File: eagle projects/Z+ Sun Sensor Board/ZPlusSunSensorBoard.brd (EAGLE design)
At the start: 78 x 78 mm, 51 parts, among them Q2 BSS138, Q4 BSS138, Q6 BSS138, Q8 BSS138, U1 ADS7841E_2K5, U2 REF194GSZ-REEL7, U3 TLV9054IDR, U4 LM20BIM7X_NOPB

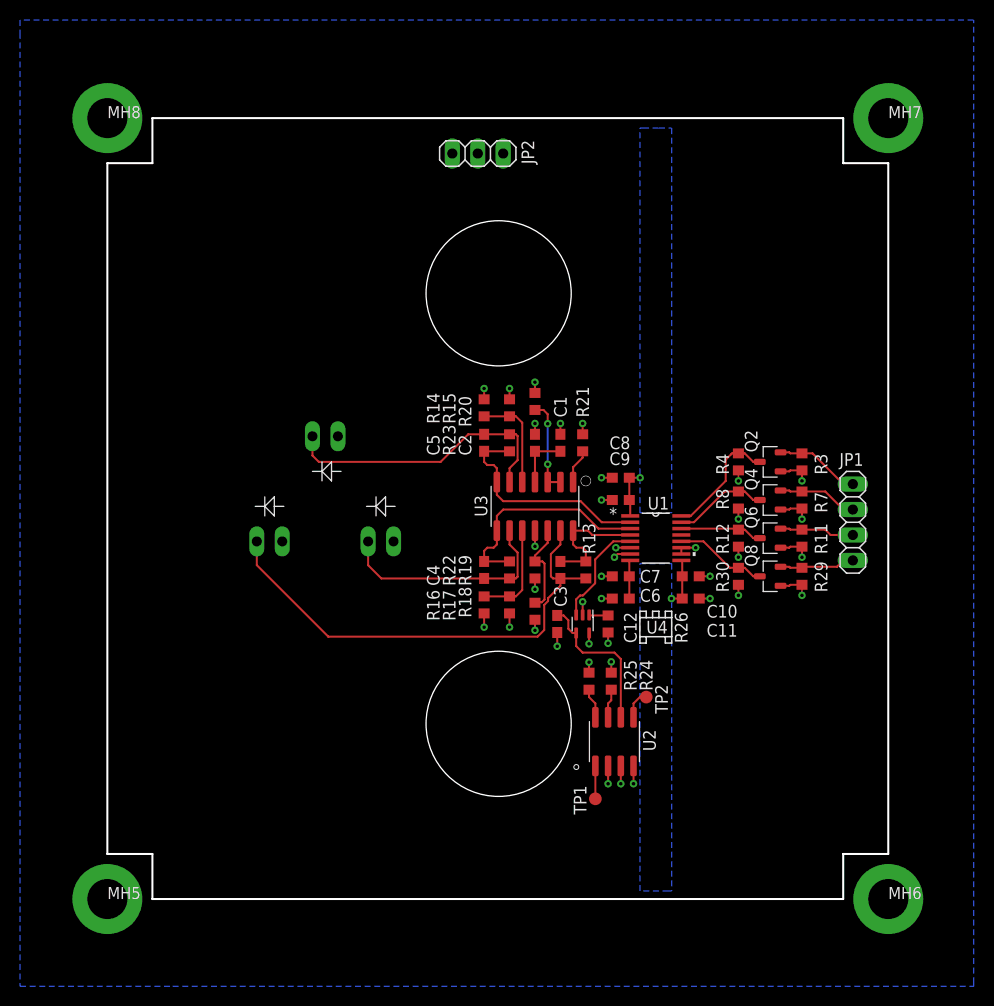
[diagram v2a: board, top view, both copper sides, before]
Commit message: New sunsensor layout and updated sun sensor mask mount
now all on 3v3 supply
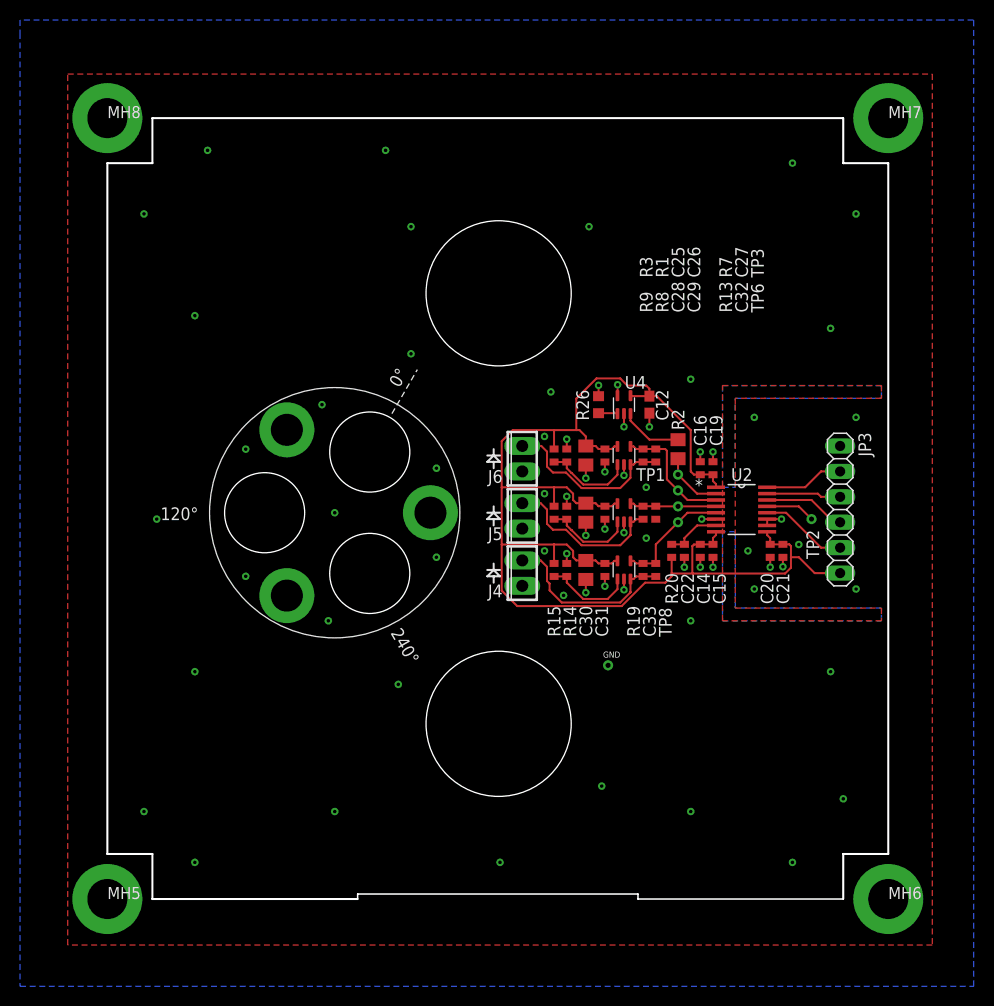
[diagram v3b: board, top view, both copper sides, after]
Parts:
- removed C1: 4.7u, rcl:C0603
- removed C10, C2, C7, C9: 0.1u, rcl:C0603
- removed C11, C6, C8: 1u, rcl:C0603
- removed C3, C4, C5: 9.1p, rcl:C0603
- removed JP1: (no value), pinhead:1X04
- removed JP2: (no value), pinhead:1X03
- removed Q2, Q4, Q6, Q8: BSS138, my_library:SOT23-3P95_237X111L42X43N_BSS138
- removed R11, R12, R29, R30, R4: 10k, rcl:R0603
- removed R16, R17, R18: 13.7k, rcl:R0603
- removed R21, R24, R25: 5.1M, rcl:R0603
- removed R22, R23: 698k, rcl:R0603
- removed U1: ADS7841E_2K5, my_library:DBQ16
- removed U3: TLV9054IDR, my_library:SOIC14P127_865X600X175L83X41N_TLV9054IDR
- added C14, C16, C21: 1u, resistor:C0402
- added C15, C19, C20, C22, C26, C29, C31: 0.1u, resistor:C0402
- added C25, C28, C30: 4.7u, rcl:C0805
- added C27, C32, C33: 0.015u, resistor:C0402
- added GND, TP3, TP6, TP8: TESTPOINT, my_library:TP_P76H50
- added J4, J5, J6: (no value), my_library:2POL254
- added JP3: (no value), pinhead:1X06
- added R1: 280R, resistor:R0402
- added R2: 0R, rcl:R0805
- added R9: 13.7k, resistor:R0402
- added U6, U8, U9: TLV9051IDCKR, my_library:SC70-5P65_210X110L36X22N_TLV9051
- A1: value SUNSENSORMASK -> SUN_SENSOR_MOUNT; device my_library:SUNSENSORMASK -> my_library:SUN_SENOR_MASK
- R13: value 698k -> 5.6k; device rcl:R0603 -> resistor:R0402
- R14: value 13.7k -> 280R; device rcl:R0603 -> resistor:R0402
- R15: device rcl:R0603 -> resistor:R0402
- R19: value 13.7k -> 5.6k; device rcl:R0603 -> resistor:R0402
- R20: value 5.1M -> 10k; device rcl:R0603 -> resistor:R0402
- R3: value 10k -> 13.7k; device rcl:R0603 -> resistor:R0402
- R7: value 10k -> 5.6k; device rcl:R0603 -> resistor:R0402
- R8: value 10k -> 280R; device rcl:R0603 -> resistor:R0402
- TP1, TP2: value TPB1,27 -> TESTPOINT; device testpad:B1,27 -> my_library:TP_P76H50
- U2: value REF194GSZ-REEL7 -> ADS7841E_2K5; device my_library:SOIC8P127_490X600X175L83X41N_REF194GSZ-REEL7 -> my_library:DBQ16
- moved TP1 33.4 mm to (63.5, 48.9)
- moved U2 26.4 mm to (69.8, 45.4)
- moved R3 24.8 mm to (51.1, 50.8), turned to 90 degrees
- moved TP2 24.3 mm to (76.8, 44.5), turned to 0 degrees
- moved C12 23.8 mm to (60.6, 55.9)
- moved U4 22.3 mm to (58.1, 55.9), turned to 0 degrees
- moved R26 21.9 mm to (55.6, 55.9), turned to 90 degrees
- moved R20 20.2 mm to (62.9, 41.3)
- moved R14 18.2 mm to (52.4, 39.4)
- moved R8 17.2 mm to (52.4, 45.1)
- moved R15 16.8 mm to (51.1, 39.4)
- moved R7 16.5 mm to (60.0, 50.8), turned to 90 degrees
- moved R19 10.8 mm to (60.0, 39.4), turned to 90 degrees
- moved R13 8.08 mm to (60.0, 45.1)
- moved A1 1.14 mm to (29.2, 45.1), flipped to the top, turned to 60 degrees
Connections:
- removed net +4V5: C12.1, C6.1, C7.1, U1.8, U2.6, U4.4
- removed net +5V: C1.1, C10.1, C11.1, C2.1, C8.1, C9.1, JP2.1, R12.2, R15.2, R17.2, R19.2, R30.2, R4.2, R8.2, U1.1, U1.7, U1.9, U2.2, U2.3, U3.4
- removed net 5V_!CS!_SUN_Z-: Q4.3, R8.1, U1.15
- removed net 5V_SPI_CLK: Q2.3, R4.1, U1.16
- removed net 5V_SPI_MISO: Q8.3, R30.1, U1.12
- removed net 5V_SPI_MOSI: Q6.3, R12.1, U1.14
- removed net IN2+BIAS: R14.2, R15.1, U3.5
- removed net IN3+BIAS: R16.2, R17.1, U3.10
- removed net IN4+BIAS: R18.2, R19.1, U3.12
- removed net N$10: TP2.TP, U2.5
- removed net N$11: TP1.TP, U2.1
- removed net N$14: A1.C2, C4.1, R22.1, U3.9
- removed net N$5: R20.2, U3.2, U3.3
- new net N$1: R2.1, U4.3
- new net N$2: TP2.1, U2.13
- new net N$3: C27.1, J6.2, R7.1, U6.3
- new net N$8: C32.1, J5.2, R13.1, U8.3
- net !CS!_SUN_Z+: now also JP3.3, U2.15; no longer JP1.2, Q4.2, R7.1
- net +3V3: now also C12.1, C14.1, C15.1, C16.1, C19.1, C20.1, C21.1, C25.1, C26.1, C28.1, C29.1, C30.1, C31.1, JP3.6, R15.2, R20.2, R9.2, U2.1, U2.8, U2.9, U4.4, U6.5, U8.5, U9.5; no longer JP2.2, Q2.1, Q4.1, Q6.1, Q8.1, R11.2, R29.2, R7.2
- net 0_DEGREES: now also C27.2, R7.2, TP3.1, U2.3, U6.4; no longer C5.2, R23.2, U1.2, U3.7
- net 120_DEGREES: now also C32.2, R13.2, TP6.1, U2.4, U8.4; no longer C4.2, R22.2, U1.3, U3.8
- net 240_DEGREES: now also C33.2, R19.2, TP8.1, U2.5, U9.4; no longer C3.2, R13.2, U1.4, U3.14
- net GND: now also C14.2, C15.2, C16.2, C19.2, C20.2, C21.2, C22.2, C25.2, C26.2, C28.2, C29.2, C30.2, C31.2, GND.1, J4.1, J5.1, J6.1, JP3.1, R1.1, R8.1, U2.10, U2.11, U2.6, U6.2, U8.2, U9.2; no longer A1.A1, A1.A2, A1.A3, C1.2, C10.2, C11.2, C2.2, C6.2, C7.2, C8.2, C9.2, JP2.3, R16.1, R18.1, R20.1, R21.2, R24.1, R25.1, U1.10, U1.11, U1.6, U2.4, U3.11
- net N$12: now also C33.1, J4.2, R19.1, U9.3; no longer R24.2, U2.7
- net N$13: now also R14.2, R15.1, U9.1; no longer R25.2, U2.8
- net N$15: now also C22.1, R20.1, U2.7; no longer A1.C3, C3.1, R13.1, U3.13
- net N$6: now also R1.2, R3.1, U6.1; no longer R21.1, U3.1
- net N$9: now also R8.2, R9.1, U8.1; no longer A1.C1, C5.1, R23.1, U3.6
- net TEMP: now also R2.2, TP1.1, U2.2; no longer U1.5, U4.3
- net UCB0_SPI_CLK: now also JP3.2, U2.16; no longer JP1.1, Q2.2, R3.1
- net UCB0_SPI_MISO: now also JP3.5, U2.12; no longer JP1.4, Q8.2, R29.1
- net UCB0_SPI_MOSI: now also JP3.4, U2.14; no longer JP1.3, Q6.2, R11.1
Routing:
- net +3V3: track 12.9 -> 138.2 mm, vias 4 -> 0
- net N$15: track 47.9 -> 5.58 mm
- net +5V: track 28.7 -> 0.00 mm, vias 12 -> 0
- net N$14: track 22.9 -> 0.00 mm
- net N$9: track 28.8 -> 9.10 mm
- net +4V5: track 19.3 -> 0.00 mm
- net N$3: track 0.00 -> 17.8 mm
- net N$8: track 0.00 -> 16.5 mm
- net N$12: track 2.89 -> 18.2 mm
- net 120_DEGREES: track 22.4 -> 8.66 mm
- net 5V_SPI_CLK: track 12.0 -> 0.00 mm
- net IN3+BIAS: track 10.0 -> 0.00 mm
- net IN2+BIAS: track 10.0 -> 0.00 mm
- net 0_DEGREES: track 22.2 -> 12.4 mm
- net N$5: track 9.54 -> 0.00 mm, vias 2 -> 0
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- added copper zone on layer 1, net GND
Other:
- outline, holes or cut-outs redrawn
